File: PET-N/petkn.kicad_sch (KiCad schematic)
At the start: 0 parts

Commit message: as sent to production
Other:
- note added: "CBM-KEYB-PETN-3.0A-20251014"
- note removed: "CBM-KEYB-PETN-3.0A-20251011"
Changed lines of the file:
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@@
 		)
 	)
-	(text "CBM-KEYB-PETN-3.0A-20251011"
+	(text "CBM-KEYB-PETN-3.0A-20251014"
 		(exclude_from_sim no)
 		(at 230.124 173.228 0)

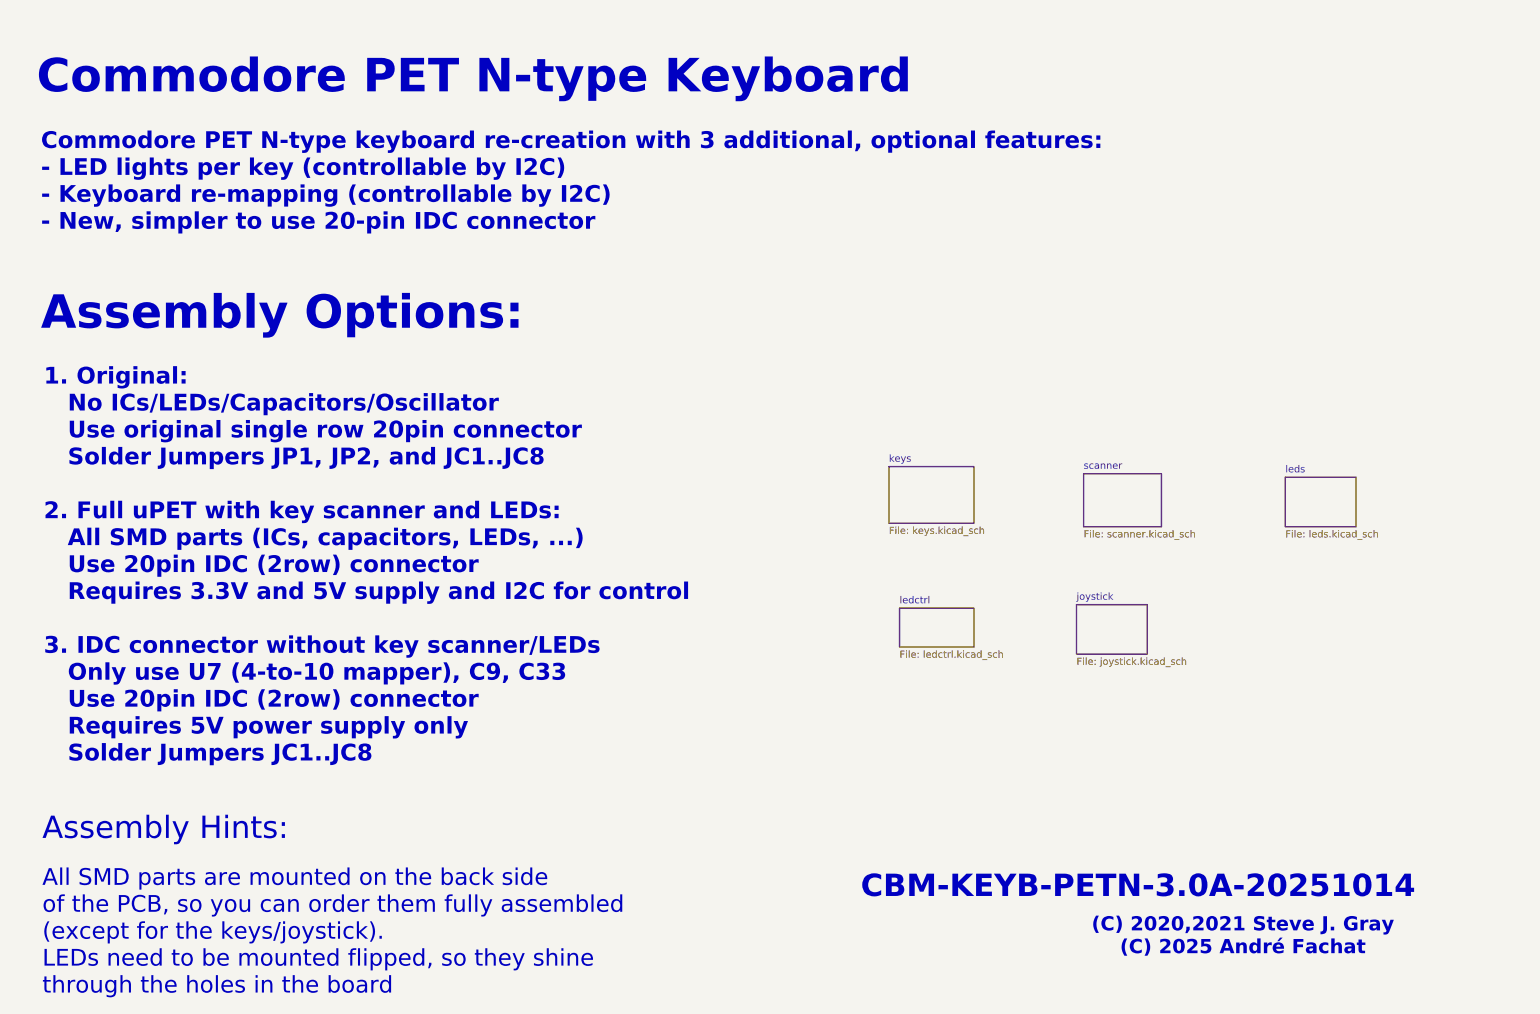
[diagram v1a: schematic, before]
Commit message: fix the two 3.0A issues (temporarily)
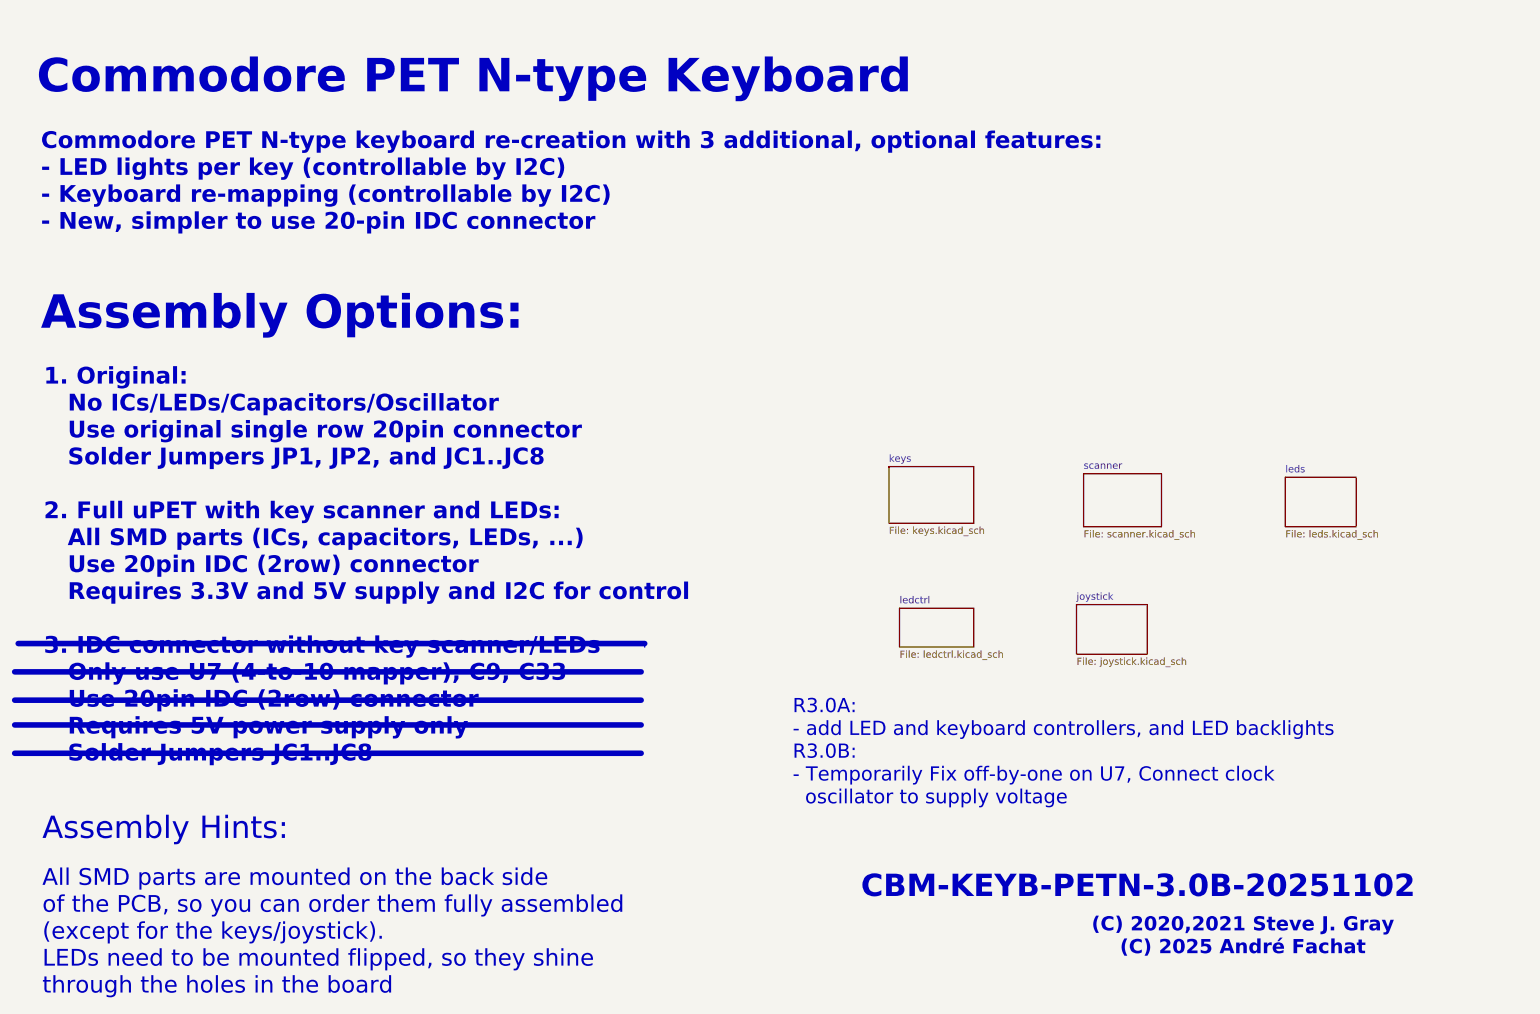
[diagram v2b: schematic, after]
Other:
- note added: "CBM-KEYB-PETN-3.0B-20251102"
- note added: "R3.0A: - add LED and keyboard controllers, and LED backlights R3.0B: - Temporarily Fix off-by-one on U7, Connect clock oscillator to supply voltage"
- note removed: "CBM-KEYB-PETN-3.0A-20251014"
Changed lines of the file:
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@@
+		)
+	)
+	(text "R3.0A:\n- add LED and keyboard controllers, and LED backlights\nR3.0B:\n- Temporarily Fix off-by-one on U7, Connect clock \n  oscillator to supply voltage"
+		(exclude_from_sim no)
+		(at 168.148 149.098 0)
+		(effects
+			(font
+				(size 2.54 2.54)
+			)
+			(justify left)
 		)
 	)
@@
 		)
 	)
-	(text "CBM-KEYB-PETN-3.0A-20251014"
+	(text "CBM-KEYB-PETN-3.0B-20251102"
 		(exclude_from_sim no)
 		(at 230.124 173.228 0)
@@
 		)
 	)
+	(polyline
+		(pts
+			(xy 141.605 129.54) (xy 141.605 130.175)
+		)
+		(stroke
+			(width 0)
+			(type default)
+		)
+	)
+	(polyline
+		(pts
+			(xy 28.575 149.225) (xy 140.97 149.225)
+		)
+		(stroke
+			(width 1)
+			(type solid)
+		)
+	)
+	(polyline
+		(pts
+			(xy 29.21 129.54) (xy 141.605 129.54)
+		)
+		(stroke
+			(width 1)
+			(type solid)
+		)
+	)
+	(polyline
+		(pts
+			(xy 28.575 134.62) (xy 140.97 134.62)
+		)
+		(stroke
+			(width 1)
+			(type solid)
+		)
+	)
+	(polyline
+		(pts
+			(xy 28.575 144.145) (xy 140.97 144.145)
+		)
+		(stroke
+			(width 1)
+			(type solid)
+		)
+	)
+	(polyline
+		(pts
+			(xy 28.575 139.7) (xy 140.97 139.7)
+		)
+		(stroke
+			(width 1)
+			(type solid)
+		)
+	)

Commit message: first run on r3.1
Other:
- added sheet connector (connector.kicad_sch)
- note added: "(C) 2020, 2021 Steve J. Gray (C) 2025, 2026 André Fachat"
- note added: "CBM-KEYB-PETN-3.1A-20260130"
- note added: "Commodore PET N-type keyboard re-creation with 4 additional, optional features: - LED lights per key (controllable by I2C) - Keyboard re-mapping (controllable by I2C) - New, simpler to use 20-pin IDC connector - Diodes to avoid mirroring"
- note added: "R4: 1U x 14 R3: 1.5U, 1U x 13 R2: 1.5U, 1U x 11, 1.5U R1: 2U, 1U x 10, 2U R1: 9U (spacebar) * Bottom 2 Rows have same profile on modern keycaps"
- note added: "RELEASES: * N-V1-R1 PCB Submitted 2020-12-18 * N-V1-R2 PCB Updated 2021-03-31 * N-V3-R1 PCB Submitted 2025-10-11 * PETN-3.1A 2026-01-30"
- note added: "Standard "N" layout with the following changes: - SPACEBAR now 6.25U. Two keys added beside it. - SHIFTLOCK is configurable - Jumpers to make extra keys work as SPACEBAR or Alternate"
- note removed: "(C) 2020,2021 Steve J. Gray (C) 2025 André Fachat"
- note removed: "CBM-KEYB-PETN-3.0B-20251102"
- note removed: "Commodore PET N-type keyboard re-creation with 3 additional, optional features: - LED lights per key (controllable by I2C) - Keyboard re-mapping (controllable by I2C) - New, simpler to use 20-pin IDC connector"
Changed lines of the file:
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@@
 	(text "1. Original:\n   No ICs/LEDs/Capacitors/Oscillator\n   Use original single row 20pin connector\n   Solder Jumpers JP1, JP2, and JC1..JC8\n\n2. Full uPET with key scanner and LEDs:\n   All SMD parts (ICs, capacitors, LEDs, ...)\n   Use 20pin IDC (2row) connector\n   Requires 3.3V and 5V supply and I2C for control\n\n3. IDC connector without key scanner/LEDs\n   Only use U7 (4-to-10 mapper), C9, C33\n   Use 20pin IDC (2row) connector\n   Requires 5V power supply only\n   Solder Jumpers JC1..JC8"
 		(exclude_from_sim no)
-		(at 33.782 115.57 0)
-		(effects
-			(font
-				(size 3 3)
+		(at 28.575 105.41 0)
+		(effects
+			(font
+				(size 2.54 2.54)
 				(thickness 0.6)
 				(bold yes)
@@
 	(text "All SMD parts are mounted on the back side\nof the PCB, so you can order them fully assembled\n(except for the keys/joystick).\nLEDs need to be mounted flipped, so they shine\nthrough the holes in the board"
 		(exclude_from_sim no)
-		(at 33.528 181.356 0)
-		(effects
-			(font
-				(size 3 3)
+		(at 31.115 173.355 0)
+		(effects
+			(font
+				(size 2.54 2.54)
 				(thickness 0.375)
 			)
@@
 		)
 	)
-	(text "Commodore PET N-type keyboard re-creation with 3 additional, optional features:\n- LED lights per key (controllable by I2C)\n- Keyboard re-mapping (controllable by I2C)\n- New, simpler to use 20-pin IDC connector"
-		(exclude_from_sim no)
-		(at 33.274 46.736 0)
-		(effects
-			(font
-				(size 3 3)
+	(text "Commodore PET N-type keyboard re-creation with 4 additional, optional features:\n- LED lights per key (controllable by I2C)\n- Keyboard re-mapping (controllable by I2C)\n- New, simpler to use 20-pin IDC connector\n- Diodes to avoid mirroring"
+		(exclude_from_sim no)
+		(at 27.94 38.735 0)
+		(effects
+			(font
+				(size 2.54 2.54)
 				(thickness 0.6)
 				(bold yes)
@@
 	(text "Assembly Options:"
 		(exclude_from_sim no)
-		(at 33.274 70.358 0)
-		(effects
-			(font
-				(size 6 6)
+		(at 29.21 67.31 0)
+		(effects
+			(font
+				(size 5.08 5.08)
 				(thickness 1.2)
 				(bold yes)
@@
 		)
 	)
-	(text "(C) 2020,2021 Steve J. Gray\n(C) 2025 André Fachat"
+	(text "RELEASES:\n* N-V1-R1 PCB Submitted 2020-12-18\n* N-V1-R2 PCB Updated 2021-03-31 \n* N-V3-R1 PCB Submitted 2025-10-11\n* PETN-3.1A 2026-01-30"
+		(exclude_from_sim no)
+		(at 133.35 76.2 0)
+		(effects
+			(font
+				(size 2.0066 2.0066)
+				(thickness 0.4013)
+				(bold yes)
+			)
+			(justify left bottom)
+		)
+	)
+	(text "(C) 2020, 2021 Steve J. Gray\n(C) 2025, 2026 André Fachat"
 		(exclude_from_sim no)
 		(at 248.92 182.118 0)
@@
 		)
 	)
+	(text "R4: 1U x 14\nR3: 1.5U, 1U x 13\nR2: 1.5U, 1U x 11, 1.5U\nR1: 2U, 1U x 10, 2U\nR1: 9U (spacebar)\n* Bottom 2 Rows have\n   same profile on modern\n   keycaps"
+		(exclude_from_sim no)
+		(at 213.36 69.215 0)
+		(effects
+			(font
+				(size 2.54 2.54)
+			)
+			(justify left bottom)
+		)
+	)
 	(text "Assembly Hints:"
 		(exclude_from_sim no)
-		(at 33.528 162.814 0)
+		(at 30.48 154.305 0)
 		(effects
 			(font
@@
 	(text "Commodore PET N-type Keyboard"
 		(exclude_from_sim no)
-		(at 32.512 27.94 0)
-		(effects
-			(font
-				(size 6 6)
+		(at 27.94 21.59 0)
+		(effects
+			(font
+				(size 5.08 5.08)
 				(thickness 1.2)
 				(bold yes)
@@
 		)
 	)
-	(text "CBM-KEYB-PETN-3.0B-20251102"
+	(text "Standard \"N\" layout with the following changes:\n- SPACEBAR now 6.25U. Two keys added beside it.\n- SHIFTLOCK is configurable\n- Jumpers to make extra keys work as SPACEBAR or Alternate\n"
+		(exclude_from_sim no)
+		(at 207.01 30.48 0)
+		(effects
+			(font
+				(size 1.5494 1.5494)
+			)
+			(justify left bottom)
+		)
+	)
+	(text "CBM-KEYB-PETN-3.1A-20260130"
 		(exclude_from_sim no)
 		(at 230.124 173.228 0)
 		(effects
 			(font
-				(size 4 4)
+				(size 3.048 3.048)
 				(thickness 0.9)
 				(bold yes)
@@
 		)
 	)
-	(polyline
-		(pts
-			(xy 28.575 149.225) (xy 140.97 149.225)
-		)
-		(stroke
-			(width 1)
-			(type solid)
-		)
-	)
-	(polyline
-		(pts
-			(xy 29.21 129.54) (xy 141.605 129.54)
-		)
-		(stroke
-			(width 1)
-			(type solid)
-		)
-	)
-	(polyline
-		(pts
-			(xy 28.575 134.62) (xy 140.97 134.62)
-		)
-		(stroke
-			(width 1)
-			(type solid)
-		)
-	)
-	(polyline
-		(pts
-			(xy 28.575 144.145) (xy 140.97 144.145)
-		)
-		(stroke
-			(width 1)
-			(type solid)
-		)
-	)
-	(polyline
-		(pts
-			(xy 28.575 139.7) (xy 140.97 139.7)
-		)
-		(stroke
-			(width 1)
-			(type solid)
-		)
-	)
 	(sheet
 		(at 185.42 97.79)
@@
 				)
 			)
+		)
+	)
+	(sheet
+		(at 255.905 122.555)
+		(size 12.7 7.62)
+		(exclude_from_sim no)
+		(in_bom yes)
+		(on_board yes)
+		(dnp no)
+		(fields_autoplaced yes)
+		(stroke
+			(width 0.1524)
+			(type solid)
+		)
+		(fill
+			(color 0 0 0 0.0000)
+		)
+		(property "Sheetname" "connector"
+			(at 255.905 121.8434 0)
+			(effects
+				(font
+					(size 1.27 1.27)
+				)
+				(justify left bottom)
+			)
+		)
+		(property "Sheetfile" "connector.kicad_sch"
+			(at 255.905 130.7596 0)
+			(effects
+				(font
+					(size 1.27 1.27)
+				)
+				(justify left top)
+			)
+		)
+		(instances
+			(project "petkn"
+				(path "/a0727808-af70-4056-b2ee-ab828c2acfbd"
+					(page "7")
+				)
+			)

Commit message: working on new layout
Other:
- note added: "Commodore PET N-type keyboard re-creation with additional, optional features: - LED lights per key (controllable by I2C) - Keyboard re-mapping (controllable by I2C) - New, simpler to use 20-pin IDC connector - Diodes to avoid mirroring"
- note removed: "Commodore PET N-type keyboard re-creation with 4 additional, optional features: - LED lights per key (controllable by I2C) - Keyboard re-mapping (controllable by I2C) - New, simpler to use 20-pin IDC connector - Diodes to avoid mirroring"
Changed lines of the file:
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@@
 	(text "1. Original:\n   No ICs/LEDs/Capacitors/Oscillator\n   Use original single row 20pin connector\n   Solder Jumpers JP1, JP2, and JC1..JC8\n\n2. Full uPET with key scanner and LEDs:\n   All SMD parts (ICs, capacitors, LEDs, ...)\n   Use 20pin IDC (2row) connector\n   Requires 3.3V and 5V supply and I2C for control\n\n3. IDC connector without key scanner/LEDs\n   Only use U7 (4-to-10 mapper), C9, C33\n   Use 20pin IDC (2row) connector\n   Requires 5V power supply only\n   Solder Jumpers JC1..JC8"
 		(exclude_from_sim no)
-		(at 28.575 105.41 0)
+		(at 29.21 106.68 0)
 		(effects
 			(font
@@
 	(text "All SMD parts are mounted on the back side\nof the PCB, so you can order them fully assembled\n(except for the keys/joystick).\nLEDs need to be mounted flipped, so they shine\nthrough the holes in the board"
 		(exclude_from_sim no)
-		(at 31.115 173.355 0)
+		(at 29.845 182.245 0)
 		(effects
 			(font
@@
 		)
 	)
-	(text "Commodore PET N-type keyboard re-creation with 4 additional, optional features:\n- LED lights per key (controllable by I2C)\n- Keyboard re-mapping (controllable by I2C)\n- New, simpler to use 20-pin IDC connector\n- Diodes to avoid mirroring"
+	(text "Commodore PET N-type keyboard re-creation with additional, optional features:\n- LED lights per key (controllable by I2C)\n- Keyboard re-mapping (controllable by I2C)\n- New, simpler to use 20-pin IDC connector\n- Diodes to avoid mirroring"
 		(exclude_from_sim no)
 		(at 27.94 38.735 0)
@@
 	(text "Assembly Hints:"
 		(exclude_from_sim no)
-		(at 30.48 154.305 0)
+		(at 29.21 163.195 0)
 		(effects
 			(font

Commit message: add orientation marker for backlight LEDs and move to 3.1B
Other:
- note added: "CBM-KEYB-PETN-3.1B-20260405"
- note added: "RELEASES: * N-V1-R1 PCB Submitted 2020-12-18 * N-V1-R2 PCB Updated 2021-03-31 * N-V3-R1 PCB Submitted 2025-10-11 * PETN-3.1A 2026-01-30 * PETN-3.1B 2026-04-05 (add orientation markers for the LEDs)"
- note removed: "CBM-KEYB-PETN-3.1A-20260130"
- note removed: "RELEASES: * N-V1-R1 PCB Submitted 2020-12-18 * N-V1-R2 PCB Updated 2021-03-31 * N-V3-R1 PCB Submitted 2025-10-11 * PETN-3.1A 2026-01-30"
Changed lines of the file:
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@@
 		)
 	)
-	(text "RELEASES:\n* N-V1-R1 PCB Submitted 2020-12-18\n* N-V1-R2 PCB Updated 2021-03-31 \n* N-V3-R1 PCB Submitted 2025-10-11\n* PETN-3.1A 2026-01-30"
+	(text "RELEASES:\n* N-V1-R1 PCB Submitted 2020-12-18\n* N-V1-R2 PCB Updated 2021-03-31 \n* N-V3-R1 PCB Submitted 2025-10-11\n* PETN-3.1A 2026-01-30\n* PETN-3.1B 2026-04-05 (add orientation \n  markers for the LEDs)"
 		(exclude_from_sim no)
 		(at 133.35 76.2 0)
@@
 		)
 	)
-	(text "CBM-KEYB-PETN-3.1A-20260130"
+	(text "CBM-KEYB-PETN-3.1B-20260405"
 		(exclude_from_sim no)
 		(at 230.124 173.228 0)
